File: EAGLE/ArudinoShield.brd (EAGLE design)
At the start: 53.3 x 59.4 mm, 25 parts, among them IC1 L298, U1 REG1117

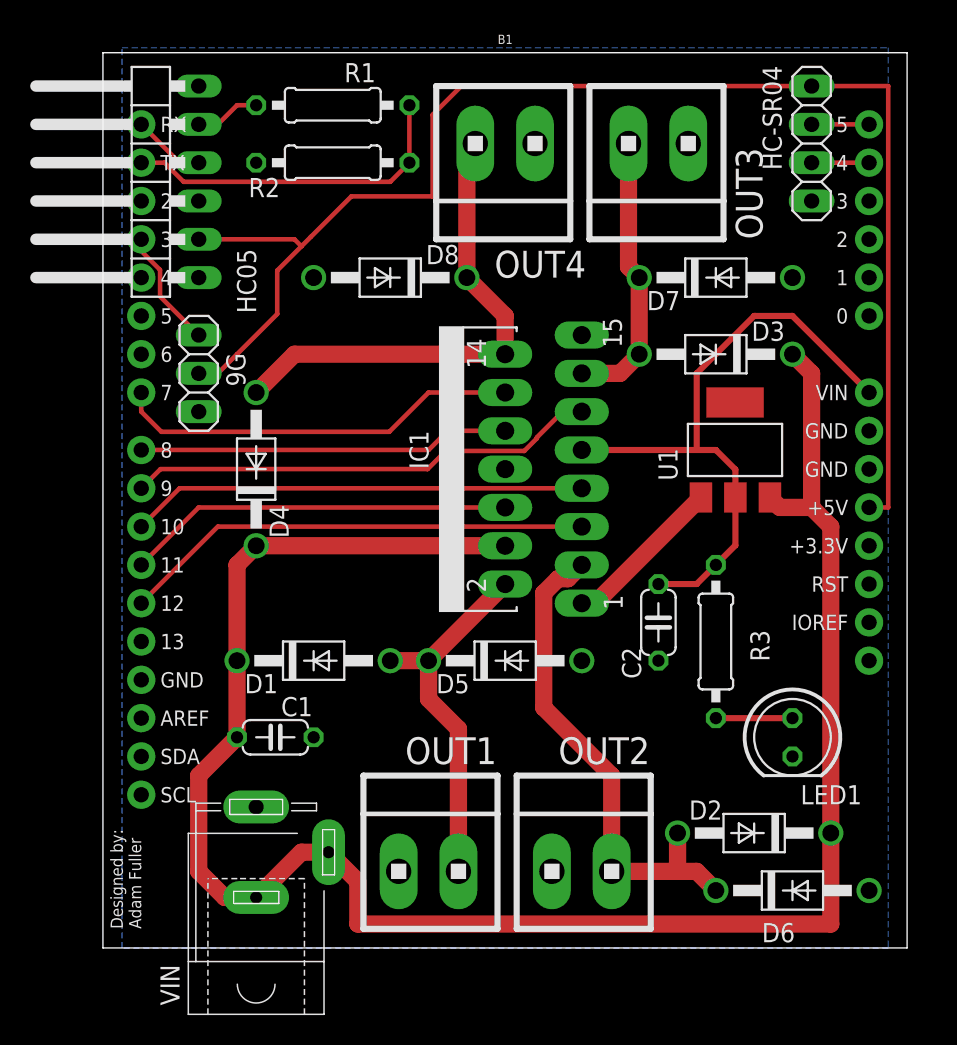
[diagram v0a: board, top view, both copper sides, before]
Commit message: updated to power peripherals from regulator, updated line width
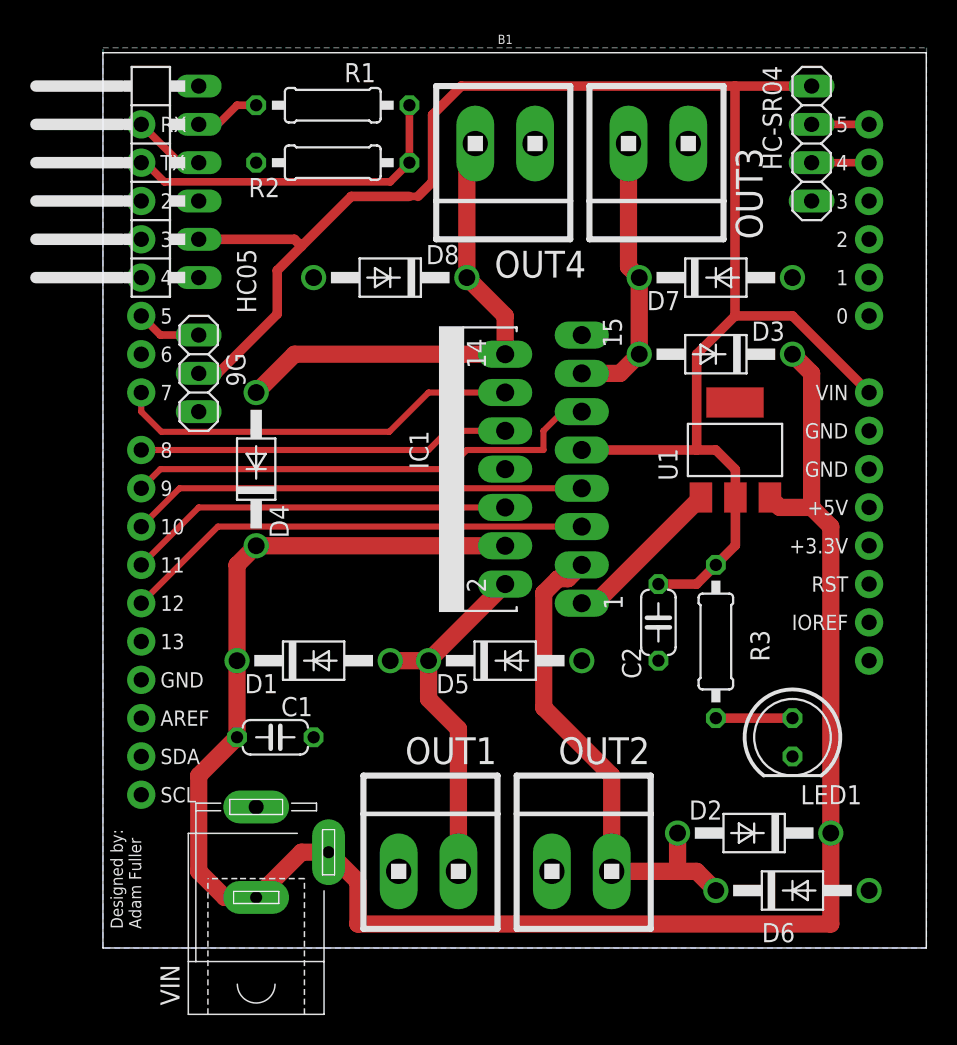
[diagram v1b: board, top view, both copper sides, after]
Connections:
- removed net +5VIN: B1.VIN, C2.1, IC1.9, R3.2, U1.2
- net +5V: now also B1.VIN, C2.1, IC1.9, R3.2, U1.2; no longer B1.5V
- net 9GPWM: now also B1.D5; no longer B1.D3
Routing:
- net +5VIN: track 42.1 -> 0.00 mm
- net +5V: track 94.7 -> 117.9 mm
- net 9GPWM: track 7.93 -> 4.34 mm
- net ENB: track 31.4 -> 32.1 mm
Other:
- board size 53.3 x 59.4 mm -> 54.6 x 59.4 mm

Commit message: updated images
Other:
- board size 54.6 x 59.4 mm -> 53.3 x 59.4 mm
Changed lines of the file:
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@@
 <board>
 <plain>
-<wire x1="34.29" y1="19.05" x2="88.88" y2="19.05" width="0" layer="20"/>
-<wire x1="88.88" y1="19.05" x2="88.88" y2="78.41" width="0" layer="20"/>
-<wire x1="88.88" y1="78.41" x2="34.29" y2="78.41" width="0" layer="20"/>
+<wire x1="34.29" y1="19.05" x2="87.61" y2="19.05" width="0" layer="20"/>
+<wire x1="87.61" y1="19.05" x2="87.61" y2="78.41" width="0" layer="20"/>
+<wire x1="87.61" y1="78.41" x2="34.29" y2="78.41" width="0" layer="20"/>
 <wire x1="34.29" y1="78.41" x2="34.29" y2="19.05" width="0" layer="20"/>
 <text x="36.83" y="20.32" size="0.8128" layer="21" rot="R90">Designed by:
@@
 <polygon width="0.508" layer="16">
 <vertex x="34.29" y="78.74"/>
-<vertex x="88.9" y="78.74"/>
-<vertex x="88.9" y="19.05"/>
+<vertex x="87.63" y="78.74"/>
+<vertex x="87.63" y="19.05"/>
 <vertex x="34.29" y="19.05"/>
 </polygon>
@@
 <contactref element="IC1" pad="11"/>
 <contactref element="B1" pad="D9"/>
-<wire x1="38.1" y1="50.8" x2="36.83" y2="49.53" width="0.4064" layer="1"/>
+<wire x1="38.1" y1="50.8" x2="36.83" y2="49.53" width="0.508" layer="1"/>
 <wire x1="66.04" y1="54.61" x2="64.77" y2="54.61" width="0.4064" layer="1"/>
 <wire x1="64.77" y1="54.61" x2="63.5" y2="53.34" width="0.4064" layer="1"/>

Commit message: minor changes
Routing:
- net VIN: track 129.0 -> 124.6 mm
- net +5V: track 117.9 -> 117.2 mm

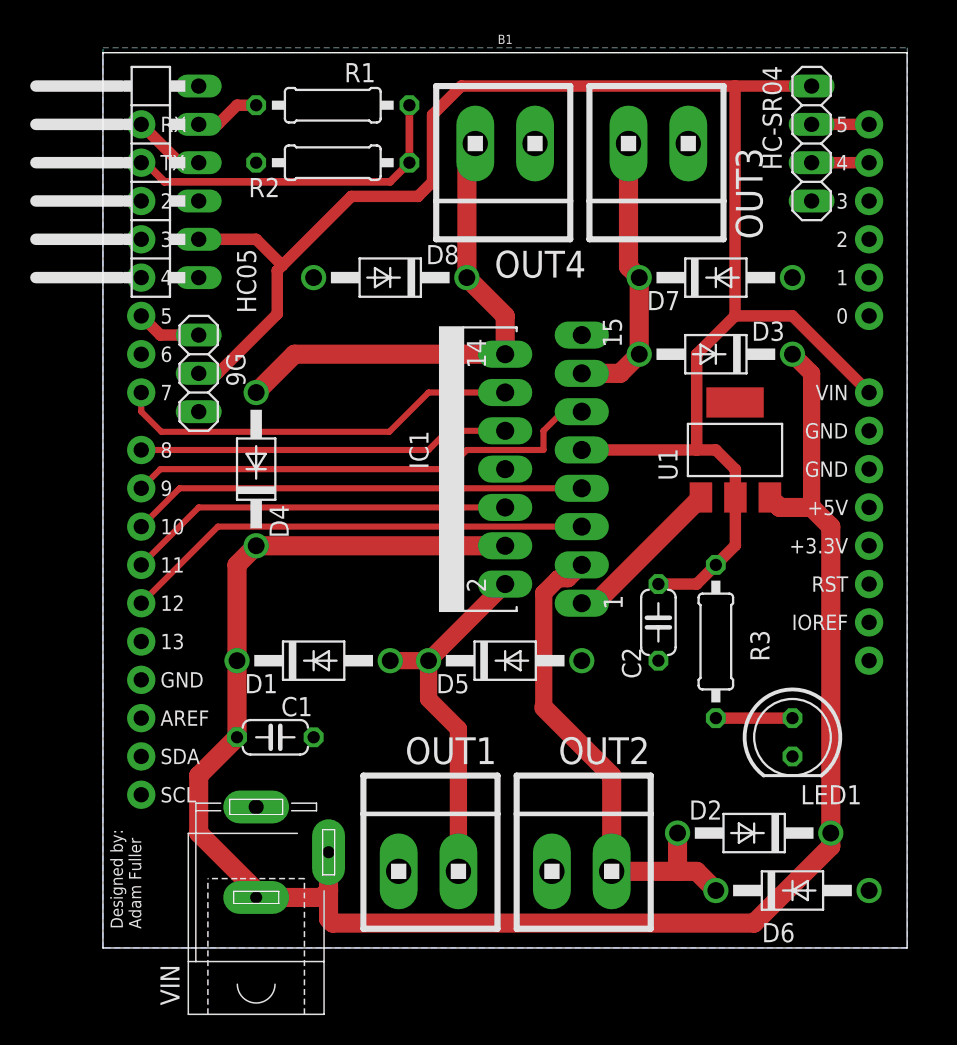
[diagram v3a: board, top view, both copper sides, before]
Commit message: moved Vin inside board
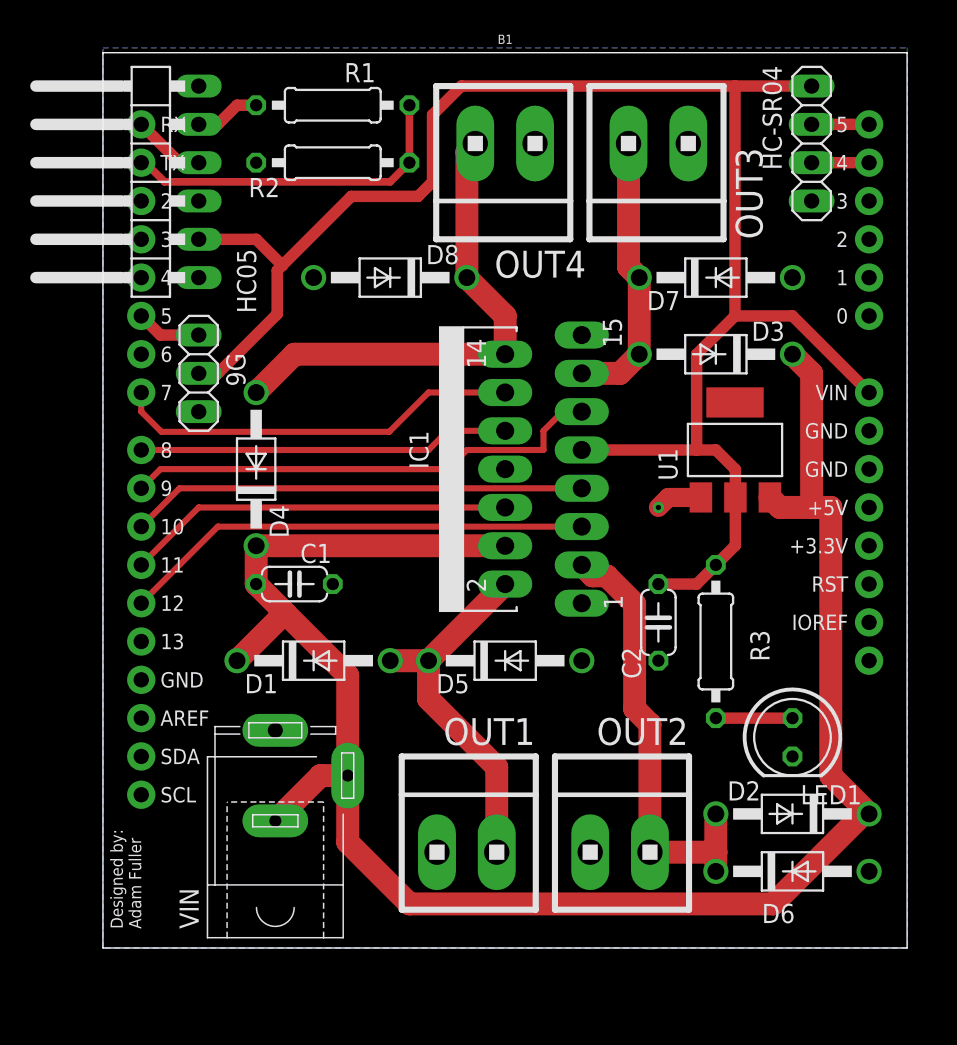
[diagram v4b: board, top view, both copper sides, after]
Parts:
- moved C1 10.2 mm to (47.0, 43.2)
- moved VIN 5.24 mm to (45.7, 30.5)
- moved D2 2.84 mm to (80.0, 27.9)
- moved OUT1 2.84 mm to (58.4, 25.4)
- moved OUT2 2.84 mm to (68.6, 25.4)
- moved D6 1.27 mm to (80.0, 24.1)
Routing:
- net GND: track 10.8 -> 3.09 mm, vias 0 -> 1
- net OUT2: track 33.6 -> 29.6 mm

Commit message: added breadboard layout
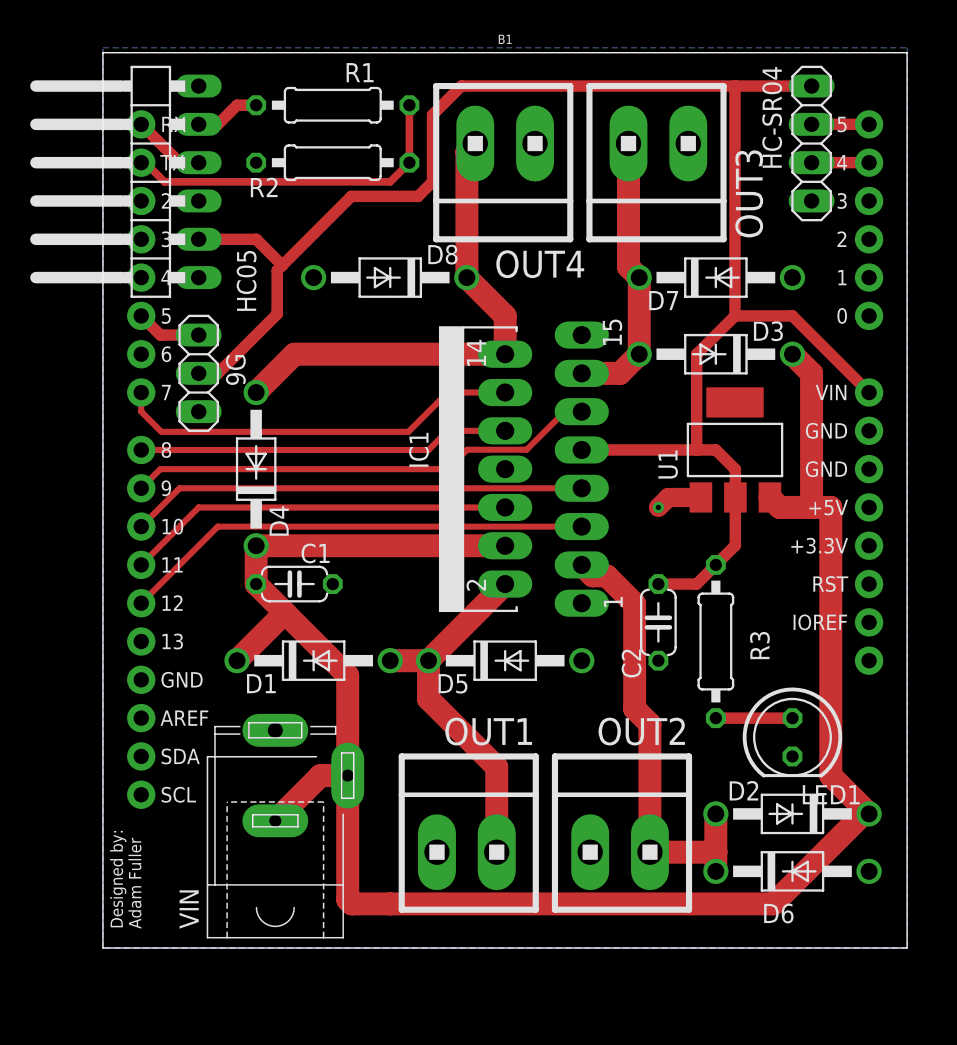
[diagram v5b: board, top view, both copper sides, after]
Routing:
- net VIN: track 124.3 -> 126.6 mm
- net ENB: track 32.1 -> 31.3 mm
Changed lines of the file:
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@@
 <wire x1="84.709" y1="27.94" x2="78.74" y2="21.971" width="1.524" layer="1"/>
 <wire x1="84.709" y1="27.94" x2="85.09" y2="27.94" width="1.27" layer="1"/>
-<wire x1="78.74" y1="21.971" x2="54.61" y2="21.971" width="1.524" layer="1"/>
+<wire x1="78.74" y1="21.971" x2="53.34" y2="21.971" width="1.524" layer="1"/>
+<wire x1="53.34" y1="21.971" x2="50.8" y2="21.971" width="1.524" layer="1"/>
 <wire x1="45.72" y1="27.48" x2="48.72" y2="30.48" width="1.524" layer="1"/>
 <wire x1="48.72" y1="30.48" x2="50.52" y2="30.48" width="1.524" layer="1"/>
@@
 <wire x1="46.355" y1="41.275" x2="44.45" y2="43.18" width="1.524" layer="1"/>
 <wire x1="44.45" y1="43.18" x2="44.45" y2="45.72" width="1.524" layer="1"/>
+<wire x1="50.8" y1="21.971" x2="50.52" y2="22.251" width="1.524" layer="1"/>
+<wire x1="50.52" y1="22.251" x2="50.52" y2="30.48" width="1.524" layer="1"/>
 <wire x1="43.18" y1="38.1" x2="46.355" y2="41.275" width="1.524" layer="1"/>
-<wire x1="54.61" y1="21.971" x2="50.52" y2="26.061" width="1.524" layer="1"/>
-<wire x1="50.52" y1="26.061" x2="50.52" y2="30.48" width="1.524" layer="1"/>
+<wire x1="53.34" y1="21.971" x2="53.34" y2="21.971" width="1.524" layer="1"/>
 </signal>
 <signal name="9GPWM">
@@
 <contactref element="B1" pad="D9"/>
 <wire x1="38.1" y1="50.8" x2="36.83" y2="49.53" width="0.4064" layer="1"/>
-<wire x1="66.04" y1="54.61" x2="64.77" y2="54.61" width="0.4064" layer="1"/>
-<wire x1="64.77" y1="54.61" x2="63.5" y2="53.34" width="0.4064" layer="1"/>
-<wire x1="63.5" y1="53.34" x2="63.5" y2="52.07" width="0.4064" layer="1"/>
-<wire x1="63.5" y1="52.07" x2="58.42" y2="52.07" width="0.4064" layer="1"/>
-<wire x1="58.42" y1="52.07" x2="57.15" y2="50.8" width="0.4064" layer="1"/>
-<wire x1="57.15" y1="50.8" x2="38.1" y2="50.8" width="0.4064" layer="1"/>
+<wire x1="38.1" y1="50.8" x2="57.15" y2="50.8" width="0.4064" layer="1"/>
+<wire x1="58.4344" y1="52.0844" x2="62.3800875" y2="52.0844" width="0.4064" layer="1"/>
+<wire x1="64.9056875" y1="54.61" x2="66.04" y2="54.61" width="0.4064" layer="1"/>
+<wire x1="62.3800875" y1="52.0844" x2="64.9056875" y2="54.61" width="0.4064" layer="1"/>
+<wire x1="57.15" y1="50.8" x2="58.4344" y2="52.0844" width="0.4064" layer="1"/>
 </signal>
 <signal name="IN2">
@@
 <wire x1="36.83" y1="55.88" x2="36.83" y2="54.61" width="0.4064" layer="1"/>
 <wire x1="38.1652" y1="53.2748" x2="36.83" y2="54.61" width="0.4064" layer="1"/>
-<wire x1="55.88" y1="55.88" x2="53.2748" y2="53.2748" width="0.4064" layer="1"/>
-<wire x1="55.88" y1="55.88" x2="60.96" y2="55.88" width="0.4064" layer="1"/>
-<wire x1="38.1652" y1="53.2748" x2="53.2748" y2="53.2748" width="0.4064" layer="1"/>
+<wire x1="57.15" y1="55.88" x2="54.5448" y2="53.2748" width="0.4064" layer="1"/>
+<wire x1="57.15" y1="55.88" x2="60.96" y2="55.88" width="0.4064" layer="1"/>
+<wire x1="38.1652" y1="53.2748" x2="54.5448" y2="53.2748" width="0.4064" layer="1"/>
 </signal>
 </signals>
